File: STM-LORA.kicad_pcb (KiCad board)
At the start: 2 copper layers, 56.5 x 50.8 mm, 22 parts, among them J1 Batt, J11 CONN_02X09, J13 CONN_01X02, J2 Solar, J3 CONN_01X17, J4 CONN_01X03, J6 CONN_01X01, J9 CONN_01X05, U1 stm32f103c8t6-module-china, U2 RFM95HW

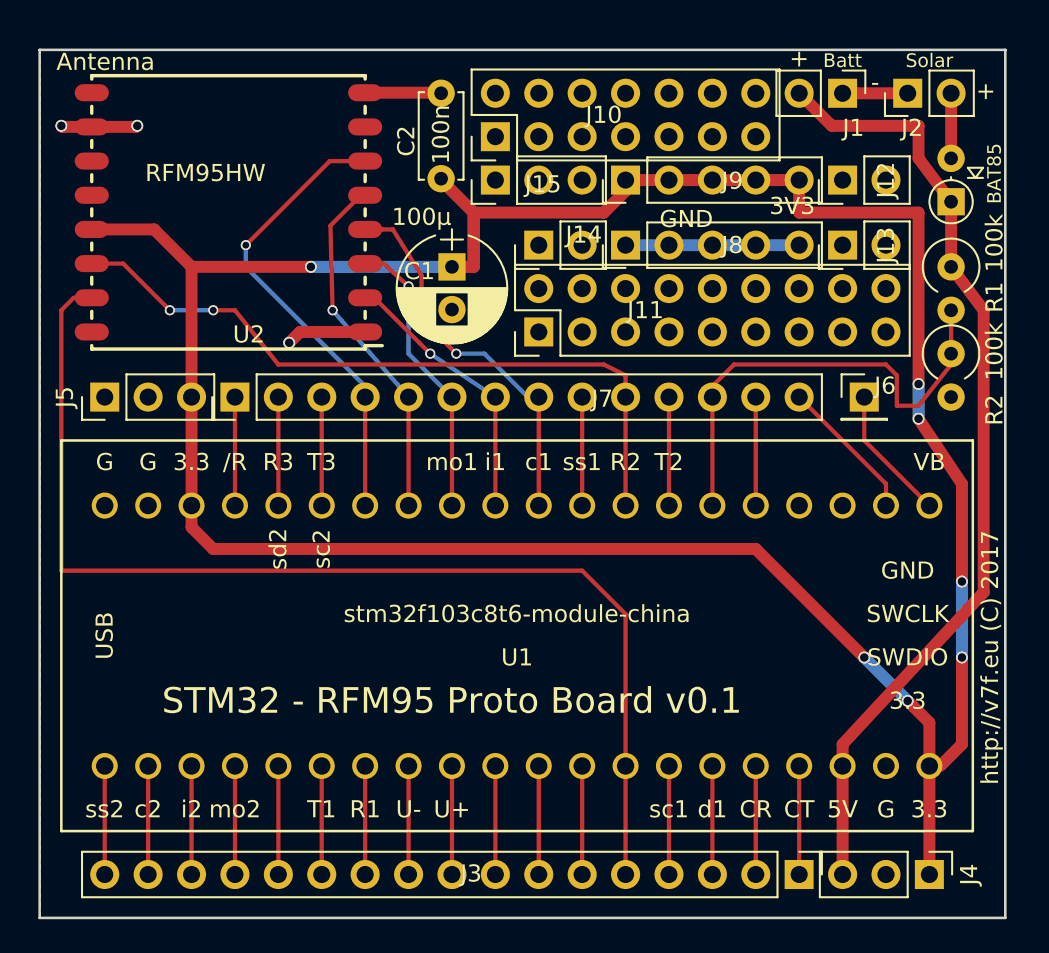
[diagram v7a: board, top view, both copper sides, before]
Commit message: add front ground plane
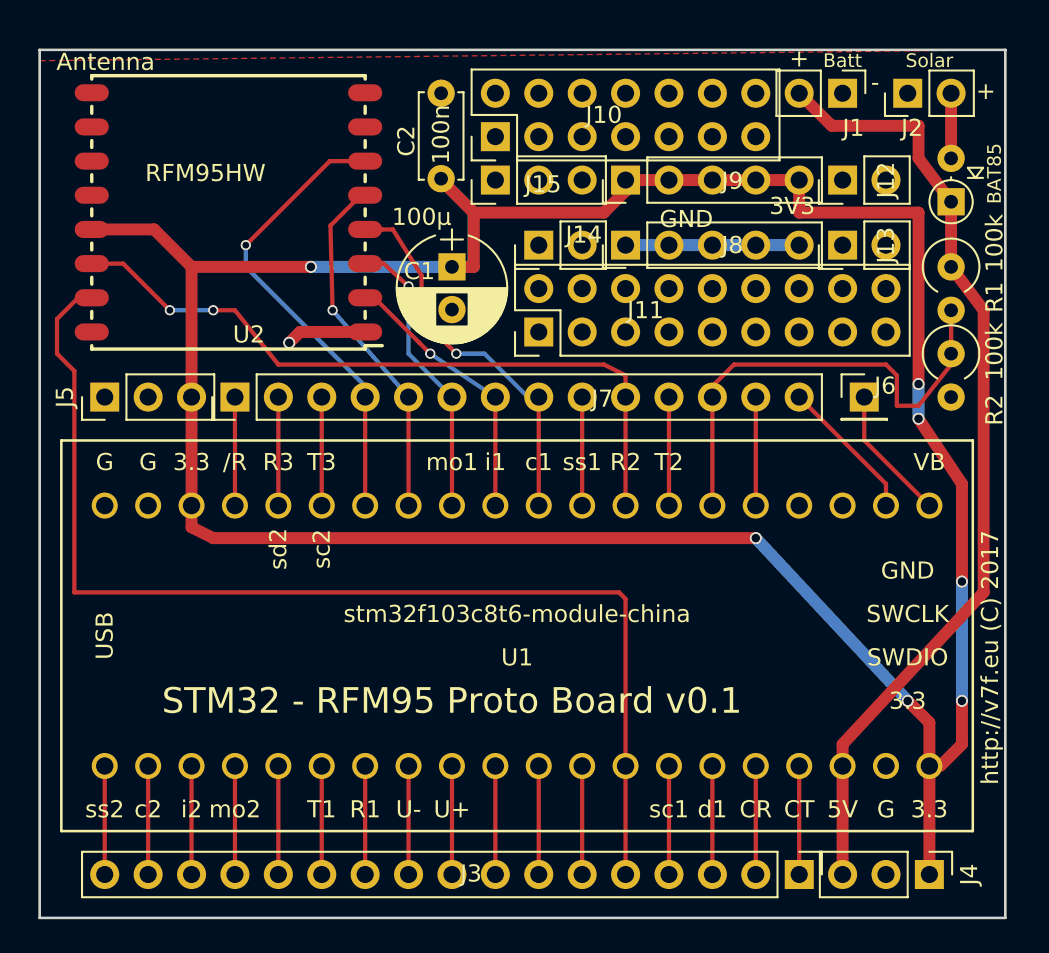
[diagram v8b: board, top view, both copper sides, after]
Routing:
- net GND: track 29.2 -> 14.9 mm, vias 3 -> 1
- net Net-(J3-Pad5): track 66.6 -> 67.5 mm
- added copper zone on F.Cu, net GND
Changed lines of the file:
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@@
     (links 75)
     (no_connects 0)
-    (area 83.744999 55.804999 140.410001 106.755001)
+    (area 83.744999 55.563 140.775 109.173333)
     (thickness 1.6)
     (drawings 12)
-    (tracks 166)
+    (tracks 157)
     (zones 0)
     (modules 22)
@@
   )
   (segment (start 128.27 67.31) (end 118.11 67.31) (width 0.7) (layer B.Cu) (net 8))
-  (segment (start 130.81 58.42) (end 134.62 58.42) (width 0.7) (layer F.Cu) (net 8) (status 30))
-  (segment (start 86.87 60.39) (end 85.155 60.39) (width 0.7) (layer F.Cu) (net 8) (status 10))
-  (via (at 85.09 60.325) (size 0.7) (drill 0.5) (layers F.Cu B.Cu) (net 8))
-  (segment (start 85.155 60.39) (end 85.09 60.325) (width 0.7) (layer F.Cu) (net 8))
-  (segment (start 86.87 60.39) (end 87.695 60.39) (width 0.7) (layer F.Cu) (net 8) (status 30))
-  (segment (start 86.87 60.39) (end 87.565 60.39) (width 0.7) (layer F.Cu) (net 8) (status 30))
-  (segment (start 86.87 60.39) (end 89.47 60.39) (width 0.7) (layer F.Cu) (net 8) (status 10))
-  (via (at 89.535 60.325) (size 0.7) (drill 0.5) (layers F.Cu B.Cu) (net 8))
-  (segment (start 89.47 60.39) (end 89.535 60.325) (width 0.7) (layer F.Cu) (net 8))
-  (segment (start 102.87 58.39) (end 107.285 58.39) (width 0.7) (layer F.Cu) (net 8) (status 30))
   (segment (start 107.285 58.39) (end 107.315 58.42) (width 0.7) (layer F.Cu) (net 8) (status 30))
   (via (at 98.425 73.025) (size 0.7) (drill 0.5) (layers F.Cu B.Cu) (net 8))
   (segment (start 102.87 72.39) (end 99.06 72.39) (width 0.7) (layer F.Cu) (net 8) (status 10))
   (segment (start 99.06 72.39) (end 98.425 73.025) (width 0.7) (layer F.Cu) (net 8))
-  (segment (start 102.9 58.42) (end 102.87 58.39) (width 0.7) (layer F.Cu) (net 8) (status 30))
   (segment (start 130.81 97.79) (end 130.81 104.14) (width 0.7) (layer F.Cu) (net 9) (status 30))
   (segment (start 135.255 60.325) (end 135.255 62.23) (width 0.7) (layer F.Cu) (net 9))
@@
   (segment (start 123.19 97.79) (end 123.19 104.14) (width 0.25) (layer F.Cu) (net 12) (status 30))
   (segment (start 120.65 97.79) (end 120.65 104.14) (width 0.25) (layer F.Cu) (net 13) (status 30))
-  (segment (start 118.11 97.79) (end 118.11 88.9) (width 0.25) (layer F.Cu) (net 14) (status 10))
-  (segment (start 85.82 70.39) (end 86.87 70.39) (width 0.25) (layer F.Cu) (net 14) (status 20))
-  (segment (start 85.09 71.12) (end 85.82 70.39) (width 0.25) (layer F.Cu) (net 14))
-  (segment (start 85.09 86.36) (end 85.09 71.12) (width 0.25) (layer F.Cu) (net 14))
-  (segment (start 115.57 86.36) (end 85.09 86.36) (width 0.25) (layer F.Cu) (net 14))
-  (segment (start 118.11 88.9) (end 115.57 86.36) (width 0.25) (layer F.Cu) (net 14))
+  (segment (start 118.11 97.79) (end 118.11 88.011) (width 0.25) (layer F.Cu) (net 14))
+  (segment (start 84.836 71.628) (end 86.074 70.39) (width 0.25) (layer F.Cu) (net 14))
+  (segment (start 84.836 73.66) (end 84.836 71.628) (width 0.25) (layer F.Cu) (net 14))
+  (segment (start 85.852 74.676) (end 84.836 73.66) (width 0.25) (layer F.Cu) (net 14))
+  (segment (start 85.852 87.63) (end 85.852 74.676) (width 0.25) (layer F.Cu) (net 14))
+  (segment (start 117.729 87.63) (end 85.852 87.63) (width 0.25) (layer F.Cu) (net 14))
+  (segment (start 118.11 88.011) (end 117.729 87.63) (width 0.25) (layer F.Cu) (net 14))
+  (segment (start 86.074 70.39) (end 86.87 70.39) (width 0.25) (layer F.Cu) (net 14))
   (segment (start 118.11 104.14) (end 118.11 97.79) (width 0.25) (layer F.Cu) (net 14) (status 30))
   (segment (start 115.57 97.79) (end 115.57 104.14) (width 0.25) (layer F.Cu) (net 15) (status 30))
@@
   (segment (start 128.27 63.5) (end 128.27 65.405) (width 0.7) (layer F.Cu) (net 27) (status 10))
   (segment (start 137.795 96.52) (end 136.525 97.79) (width 0.7) (layer F.Cu) (net 27) (status 20))
-  (segment (start 137.795 91.44) (end 137.795 96.52) (width 0.7) (layer F.Cu) (net 27))
-  (via (at 137.795 91.44) (size 0.7) (drill 0.5) (layers F.Cu B.Cu) (net 27))
-  (segment (start 137.795 86.995) (end 137.795 91.44) (width 0.7) (layer B.Cu) (net 27))
+  (segment (start 137.795 93.98) (end 137.795 96.52) (width 0.7) (layer F.Cu) (net 27))
+  (via (at 137.795 93.98) (size 0.7) (drill 0.5) (layers F.Cu B.Cu) (net 27))
+  (segment (start 137.795 86.995) (end 137.795 93.98) (width 0.7) (layer B.Cu) (net 27))
   (via (at 137.795 86.995) (size 0.7) (drill 0.5) (layers F.Cu B.Cu) (net 27))
   (segment (start 137.795 81.28) (end 137.795 86.995) (width 0.7) (layer F.Cu) (net 27))
@@
   (segment (start 135.89 97.79) (end 135.89 95.25) (width 0.7) (layer F.Cu) (net 27) (status 10))
   (segment (start 92.71 83.82) (end 92.71 82.55) (width 0.7) (layer F.Cu) (net 27) (status 20))
-  (segment (start 93.98 85.09) (end 92.71 83.82) (width 0.7) (layer F.Cu) (net 27))
-  (segment (start 125.73 85.09) (end 93.98 85.09) (width 0.7) (layer F.Cu) (net 27))
-  (segment (start 132.08 91.44) (end 125.73 85.09) (width 0.7) (layer F.Cu) (net 27))
-  (via (at 132.08 91.44) (size 0.7) (drill 0.5) (layers F.Cu B.Cu) (net 27))
-  (segment (start 134.62 93.98) (end 132.08 91.44) (width 0.7) (layer B.Cu) (net 27))
+  (segment (start 93.98 84.455) (end 92.71 83.82) (width 0.7) (layer F.Cu) (net 27))
+  (segment (start 125.73 84.455) (end 93.98 84.455) (width 0.7) (layer F.Cu) (net 27))
+  (segment (start 125.73 84.455) (end 125.73 84.455) (width 0.7) (layer F.Cu) (net 27))
+  (via (at 125.73 84.455) (size 0.7) (drill 0.5) (layers F.Cu B.Cu) (net 27))
+  (segment (start 134.62 93.98) (end 125.73 84.455) (width 0.7) (layer B.Cu) (net 27))
   (via (at 134.62 93.98) (size 0.7) (drill 0.5) (layers F.Cu B.Cu) (net 27))
   (segment (start 135.89 95.25) (end 134.62 93.98) (width 0.7) (layer F.Cu) (net 27))
@@
       )
     )
+  )
+  (zone (net 8) (net_name GND) (layer F.Cu) (hatch edge 0.508)
+    (connect_pads (clearance 0.508))
+    (min_thickness 0.254)
+    (fill yes (arc_segments 16) (thermal_gap 0.508) (thermal_bridge_width 0.508))
+    (polygon
+      (pts
+        (xy 140.335 106.68) (xy 83.82 106.68) (xy 83.82 56.515) (xy 140.335 55.88)
+      )
+    )
